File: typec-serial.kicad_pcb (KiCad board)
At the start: 2 copper layers, 12 x 26.8 mm, 16 parts, among them IC1 NJM12888F33-TE1, J1 USB4085-GF-A_REVB, J2 Conn_01x04_Pin, U1 FT230XS

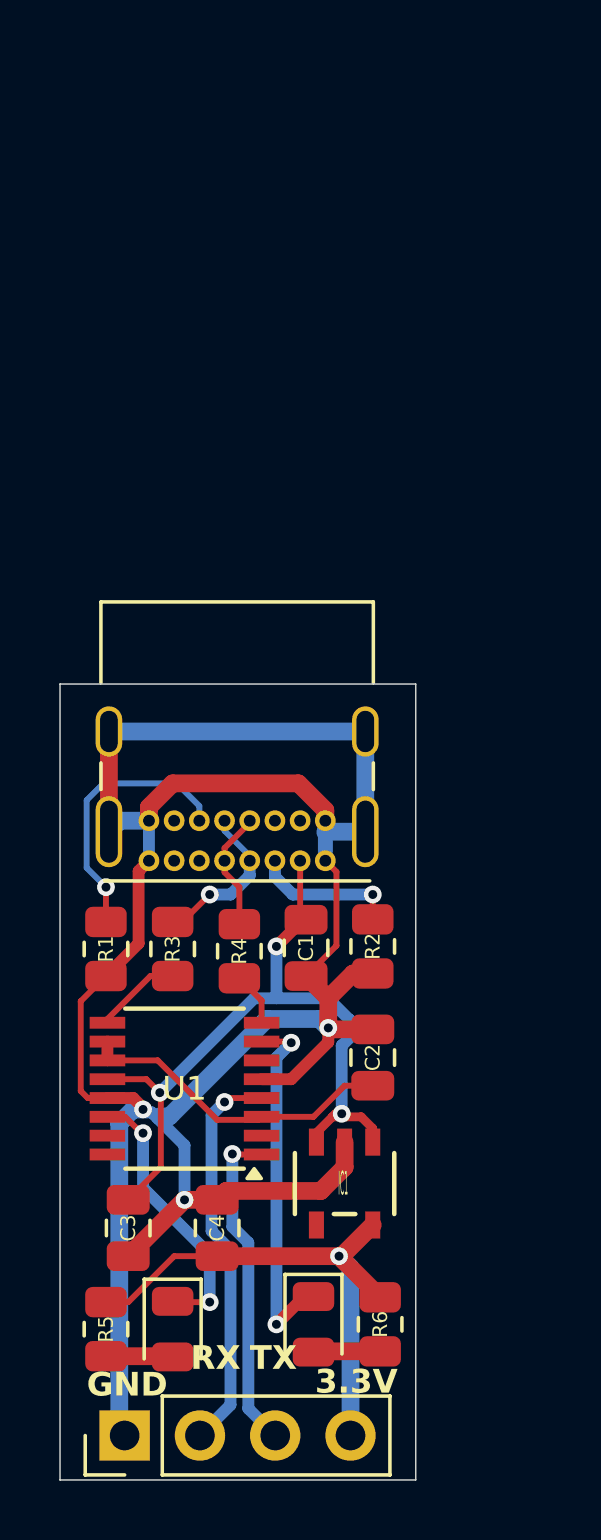
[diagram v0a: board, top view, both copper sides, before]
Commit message: :fire: remove regulator
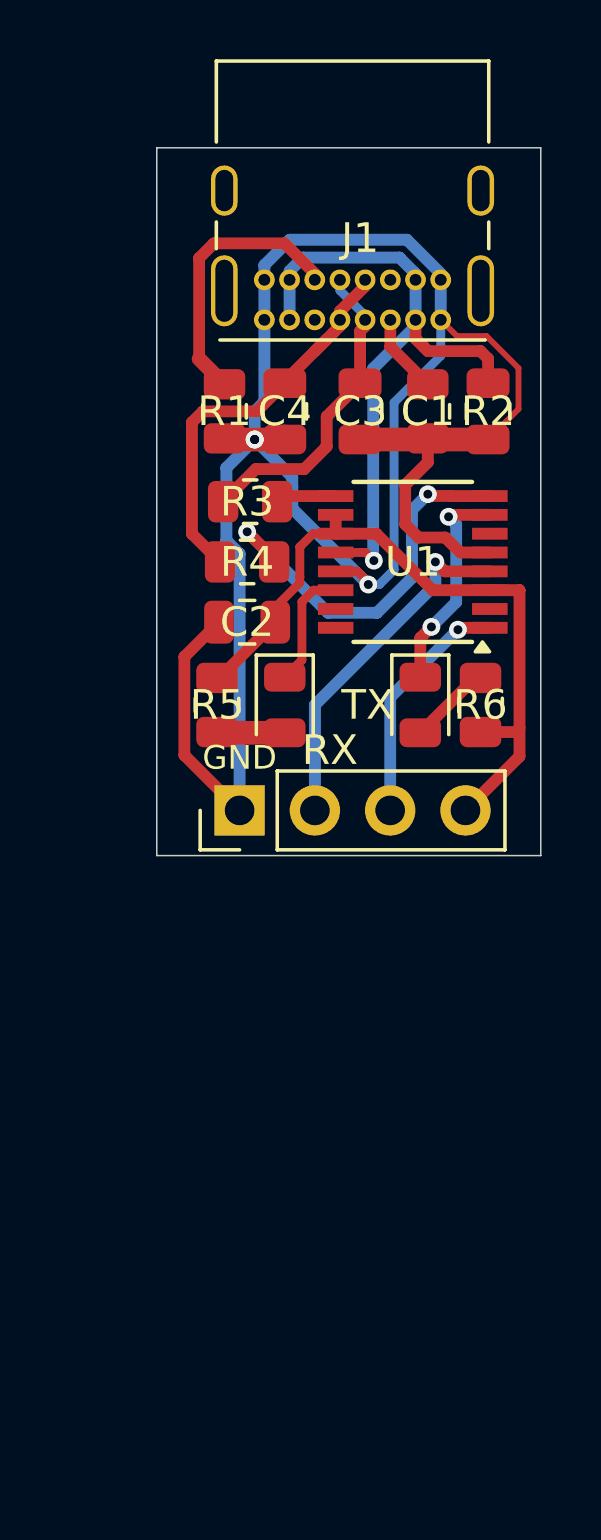
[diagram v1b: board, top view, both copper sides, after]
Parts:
- removed D1, D2: ~, LED_SMD:LED_0805_2012Metric
- removed IC1: NJM12888F33-TE1, footprints:PI-SOT-23-5-E-A_NMD
- removed J2: Conn_01x04_Pin, Connector_PinHeader_2.54mm:PinHeader_1x04_P2.54mm_Vertical
- added GND: Conn_01x04_Pin, Connector_PinHeader_2.54mm:PinHeader_1x04_P2.54mm_Vertical, F.Cu at (159.3, 89.7)
- added RX: ~, LED_SMD:LED_0805_2012Metric, F.Cu at (160.8, 86.1)
- added TX: ~, LED_SMD:LED_0805_2012Metric, F.Cu at (165.4, 86.1)
- C3: value 0.1u -> C
- C4: value 0.47u -> C
- R5, R6: value 1k -> 470
- moved C3 28.6 mm to (163.3, 76.2), turned to -90 degrees
- moved C4 27.6 mm to (160.8, 76.2)
- moved R5 21.4 mm to (158.5, 86.1)
- moved R6 21.2 mm to (167.4, 86.1), turned to -90 degrees
- moved U1 19.4 mm to (165.1, 81.3)
- moved C1 19.1 mm to (167.6, 76.2)
- moved J1 18.7 mm to (166.0, 73.1)
- moved R1 18.6 mm to (158.8, 76.2)
- moved R2 18.1 mm to (165.6, 76.2)
- moved R3 15.3 mm to (159.6, 79.2), turned to 0 degrees
- moved C2 15.3 mm to (159.5, 83.3), turned to 0 degrees
- moved R4 13.1 mm to (159.5, 81.3), turned to 0 degrees
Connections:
- C1 pad 2: Net-(IC1-CONTROL) -> Net-(J1-VBUS)
- C2 pad 2: Net-(U1-3V3OUT) -> Net-(J2-Pin_4)
- C3 pad 1: GND -> Net-(J1-DP1)
- C3 pad 2: Net-(IC1-CONTROL) -> GND
- C4 pad 1: GND -> Net-(J1-DN1)
- C4 pad 2: Net-(IC1-VOUT) -> GND
- J1 pad A4: Net-(IC1-CONTROL) -> Net-(J1-VBUS)
- J1 pad A9: unconnected-(J1-VBUS__1-PadA9) -> Net-(J1-VBUS)
- J1 pad B4: unconnected-(J1-VBUS__2-PadB4) -> Net-(J1-VBUS)
- J1 pad B9: unconnected-(J1-VBUS__3-PadB9) -> Net-(J1-VBUS)
- J1 pad S1: GND -> unconnected-(J1-SHELL-PadS1)_3
- R5 pad 1: Net-(IC1-VOUT) -> Net-(J2-Pin_4)
- R6 pad 2: Net-(IC1-VOUT) -> Net-(J2-Pin_4)
- U1 pad 10: Net-(U1-3V3OUT) -> Net-(J2-Pin_4)
- U1 pad 11: Net-(U1-3V3OUT) -> Net-(J2-Pin_4)
- U1 pad 12: Net-(IC1-CONTROL) -> Net-(J1-VBUS)
- U1 pad 3: Net-(U1-3V3OUT) -> Net-(J2-Pin_4)
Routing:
- net Net-(IC1-CONTROL): track 25.9 -> 0.00 mm, vias 3 -> 0
- net Net-(J2-Pin_4): track 0.00 -> 24.4 mm
- net Net-(J1-VBUS): track 0.00 -> 22.2 mm, vias 0 -> 1
- net Net-(IC1-VOUT): track 18.3 -> 0.00 mm, vias 1 -> 0
- net Net-(U1-USBDP): track 1.81 -> 13.7 mm, vias 0 -> 2
- net GND: track 84.6 -> 72.7 mm
- net Net-(U1-3V3OUT): track 10.9 -> 0.00 mm
- net Net-(J1-DN1): track 4.40 -> 14.6 mm
- net Net-(J1-DP1): track 5.45 -> 10.8 mm, vias 1 -> 0
- net Net-(D1-K): track 9.31 -> 4.09 mm, vias 2 -> 0
- net Net-(D2-K): track 12.4 -> 7.44 mm
- net Net-(J2-Pin_3): track 11.1 -> 8.15 mm
- net Net-(J1-CC1): track 4.92 -> 2.84 mm, vias 1 -> 0
- net Net-(J2-Pin_2): track 13.4 -> 12.0 mm
- net Net-(U1-USBDM): track 2.93 -> 2.05 mm
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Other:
- board size 12 x 26.8 mm -> 13 x 23.9 mm
- board text added: "2025/03/10 K.Kamura"
- board text removed: "3.3V"
- board text removed: "GND"
- board text removed: "K.Kamura 2025.03.08"
- board text removed: "RX"
- board text removed: "TX"
